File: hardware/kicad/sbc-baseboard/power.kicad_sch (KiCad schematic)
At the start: 86 parts, among them J17 Qwiic PD programming, J2 USB-C PD in, Q101 2N7002, Q102 2N7002, U101 STUSB4500QTR, U102 PCA9517A, U103 TPS54560BDDA, U104 TPS54560BDDA, U105 TPS62823DLC

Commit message: Re-lay out every sheet around its main component
Nets fan out of each hub IC as wires at pin pitch; connectors, series
parts, pull-ups and power symbols sit at the lane ends, and labels are
kept for nets that leave the page. Supply pins share a bus with their
decoupling; ESD arrays sit on the connector's D-/D+ rows and port
switches on the VBUS row, so every wire into a receptacle is straight;
the stacked USB-A is a two-unit symbol, one per port. Relays move to
their own sheet (8xx). ESD diodes use KiCad's PESD5V0S1UL in SOD-882.

Generator: gen/fanout.py (lane engine), gen/check_geom.py (endpoint
contacts), gen/netcheck.py (wire-level rail merges). ERC, both checks
and a renumbering-tolerant netlist diff against the first pass all
clean; 331 parts, 354 nets.

Co-Authored-By: Claude Fable 5.1 <noreply@anthropic.com>
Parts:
- removed C117, C126: 100u/10V, Capacitor_SMD:CP_Elec_8x10.5, symbol Device:C_Polarized
- removed C119, C128: 47u/10V, Capacitor_SMD:C_1210_3225Metric, symbol Device:C
- removed C132: 22u, Capacitor_SMD:C_0805_2012Metric, symbol Device:C
- removed D101: SMAJ24A, Diode_SMD:D_SMA, symbol Diode:SMAJ24A
- removed D102, D110, D112: LED AMBER, LED_SMD:LED_0603_1608Metric, symbol Device:LED
- removed D105: BZT52C5V1, Diode_SMD:D_SOD-123, symbol Device:D_Zener
- removed D106, D107: PESD5V0S1UL, Diode_SMD:D_SOD-523, symbol Device:D_TVS
- removed D108: BAT54C, Package_TO_SOT_SMD:SOT-23, symbol Diode:BAT54C
- removed D111, D113: B560C, Diode_SMD:D_SMA, symbol Device:D_Schottky
- added C117, C126: 47u/10V, Capacitor_SMD:C_1210_3225Metric, symbol Device:C
- added C119, C128: 100u/10V, Capacitor_SMD:CP_Elec_8x10.5, symbol Device:C_Polarized
- added D101: BAT54C, Package_TO_SOT_SMD:SOT-23, symbol Diode:BAT54C
- added D102: ESDA25W, Diode_SMD:D_SOD-523, symbol Device:D_TVS
- added D105, D111, D113: LED AMBER, LED_SMD:LED_0603_1608Metric, symbol Device:LED
- added D106, D107: PESD5V0S1UL, Diode_SMD:D_SOD-882, symbol Diode:PESD5V0S1UL
- added D108: BZT52C5V1, Diode_SMD:D_SOD-123, symbol Device:D_Zener
- added D110, D112: B560C, Diode_SMD:D_SMA, symbol Device:D_Schottky
- C105: value 100n/50V -> 1u
- C108: value 1u -> 100n
- C111: value 100n -> 100n/50V
- C114, C123: value 100n/50V -> 47p
- C116, C125: value 47p -> 100n/50V
- C118, C127: value 100n/50V -> 47u/10V; footprint Capacitor_SMD:C_0603_1608Metric -> Capacitor_SMD:C_1210_3225Metric
- C120: value 47u/10V -> 100n/50V; footprint Capacitor_SMD:C_1210_3225Metric -> Capacitor_SMD:C_0603_1608Metric
- C129: value 47u/10V -> 10u; footprint Capacitor_SMD:C_1210_3225Metric -> Capacitor_SMD:C_0805_2012Metric
- C130: value 10u -> 22u
- D104: value ESDA25W -> SMAJ24A; footprint Diode_SMD:D_SOD-523 -> Diode_SMD:D_SMA
- R103: value 470 -> 10k; footprint Resistor_SMD:R_1206_3216Metric -> Resistor_SMD:R_0603_1608Metric
- R105: value 100k -> 4.7k
- R106: value 10k -> 4.7k
- R108: value 4.7k -> 100k
- R109: value 4.7k -> 470; footprint Resistor_SMD:R_0603_1608Metric -> Resistor_SMD:R_1206_3216Metric
- R110: value 100k -> 10k
- R111, R128: value 470 -> 100k
- R114, R126: value 100k -> 470
- R115: value 10k -> 100k
- R116, R121: value 243k -> 19.1k
- R117, R122: value 19.1k -> 243k
- R118, R123: value 51.1k -> 9.76k
- R119, R124: value 9.76k -> 51.1k
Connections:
- net +3V3: now also C110.1, C130.1, R102.1, R128.2, D101.1; no longer C111.1, R115.1, R128.1
- net +3V3_PD: now also C108.1, R105.1, R110.1, R114.1, D101.3; no longer C110.1, R108.1, R109.1, R111.1
- net +3V3_PRG: now also C107.1, R112.2, R115.1, D101.2; no longer C108.1, R105.1, R112.1
- net +5V_PORTS: now also C118.1, C129.1, R119.2, C117.1, C119.1; no longer C120.1, C130.1, R118.1
- net +5V_TGT: now also C127.1, R124.2, C126.1, C128.1; no longer C129.1, R123.1
- net GND: now also C118.2, C127.2, D103.1 (A1), D104.1 (A1), R103.2, R111.2, R113.2, R117.2, R118.2, R122.2, R123.2, C117.2, C119.2, C126.2, C128.2, D102.1 (A1), D105.1 (K), D106.2 (A), D107.2 (A), D108.2 (A), D110.2 (A), D111.1 (K), D112.2 (A), D113.1 (K); no longer C116.2, C125.2, D103.2 (A2), D104.2 (A2), R102.2, R105.2, R114.2, R116.2, R119.2, R121.2, R124.2
- net PD_ATTACH_N: now also R110.2; no longer R106.2
- net PD_PROG_DET: now also R115.2; no longer R112.2
- net VBUS_IN: now also C111.1, C120.1, D104.2 (A2), R104.2, R108.1, R109.2; no longer C105.1, C114.1, C123.1, R103.1, R104.1, R110.1
- net at D114.2 (A): now also R126.2; no longer R128.2
- net at R101.2: now also D105.2 (A)
- net at D109.2 (A): now also R114.2; no longer R111.2
- net at R125.2: now also D113.2 (A)
- net at R120.2: now also D111.2 (A)
- net PCA_EN: no longer names the net of Q102.3 (D), U102.5 (EN)
- net PCA_EN: now also R102.2; no longer R115.2
- removed net PCA_EN_GATE: Q102.1 (G), R113.2, R114.1
- net PD_CC1: no longer names the net of J2.A5 (CC1), U101.1 (CC1DB), U101.2 (CC1)
- net PD_CC1: now also D102.2 (A2); no longer D103.1 (A1)
- net PD_CC2: no longer names the net of J2.B5 (CC2), U101.4 (CC2), U101.5 (CC2DB)
- net PD_CC2: now also D103.2 (A2); no longer D104.1 (A1)
- net PD_DISCH: no longer names the net of U101.9 (DISCH)
- net PD_DISCH: now also R109.1; no longer R103.2
- net PD_RESET: no longer names the net of U101.6 (RESET)
- net PD_RESET: now also R103.1; no longer R102.1
- net PD_SCL: no longer names the net of J17.4 (Pin_4), U101.7 (SCL), U102.2 (SCLA)
- net PD_SCL: now also R105.2, D106.1 (K); no longer R108.2
- net PD_SDA: no longer names the net of J17.3 (Pin_3), U101.8 (SDA), U102.3 (SDAA)
- net PD_SDA: now also R106.2, D107.1 (K); no longer R109.2
- net PD_VBUS_EN_N: no longer names the net of Q101.1 (G), U101.16 (VBUS_EN_SNK)
- net PD_VBUS_EN_N: now also R108.2, D108.1 (K); no longer R110.2
- net PD_VBUS_VS: no longer names the net of U101.18 (VBUS_VS_DISCH)
- net PD_VBUS_VS: now also R104.1; no longer R104.2
- net PD_VREG_1V2: no longer names the net of U101.21 (VREG_1V2)
- net PD_VREG_1V2: now also C105.1; no longer C106.1
- net PD_VREG_2V7: no longer names the net of U101.23 (VREG_2V7)
- net PD_VREG_2V7: now also C106.1; no longer C107.1
- net U103_BOOT: no longer names the net of U103.1 (BOOT)
- net U103_BOOT: now also C116.1; no longer C118.1
- removed net U103_COMP: C116.1, R117.1, U103.6 (COMP)
- net U103_CZ: no longer names the net of C115.1
- net U103_CZ: now also R116.2; no longer R117.2
- net U103_FB: no longer names the net of R119.1, U103.5 (FB)
- net U103_FB: now also R118.1; no longer R118.2
- net U103_RT: no longer names the net of R116.1
- net U103_RT: now also C114.1, U103.6 (COMP); no longer U103.4 (RT/CLK)
- net U103_SW: no longer names the net of L101.1, U103.8 (SW)
- net U103_SW: now also C116.2, D110.1 (K); no longer C118.2
- net U104_BOOT: no longer names the net of U104.1 (BOOT)
- net U104_BOOT: now also C125.1; no longer C127.1
- removed net U104_COMP: C125.1, R122.1, U104.6 (COMP)
- net U104_CZ: no longer names the net of C124.1
- net U104_CZ: now also R121.2; no longer R122.2
- net U104_FB: no longer names the net of R124.1, U104.5 (FB)
- net U104_FB: now also R123.1; no longer R123.2
- net U104_RT: no longer names the net of R121.1
- net U104_RT: now also C123.1, U104.6 (COMP); no longer U104.4 (RT/CLK)
- net U104_SW: no longer names the net of L102.1, U104.8 (SW)
- net U104_SW: now also C125.2, D112.1 (K); no longer C127.2
- net U105_FB: no longer names the net of R127.1, U105.2 (FB)
- net U105_FB: now also R128.1; no longer R126.2
- net U105_SW: no longer names the net of L103.1, U105.6 (SW)
- new net: Q102.1 (G), R111.1, R112.1
- new net: R117.1, U103.4 (RT/CLK)
- new net: R122.1, U104.4 (RT/CLK)
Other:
- note added: "A programmer on J17 pulls PCA_EN low through Q102: the K64 is disconnected from the PD bus in hardware."
- note added: "J2 is a PD sink only (no data). STUSB4500 negotiates from NVM; VBUS_EN_SNK gates the 5 V bucks through Q101,"
- note added: "The zener keeps the gate under 5.1 V at 20 V VBUS."
- note removed: "A programmer on J17 pulls PCA_EN low: the K64 is disconnected from the PD bus in hardware."
- note removed: "Buck 1 feeds the USB ports, the FT231X, the relay coils and buck 3 (~4.6 A at 1.0 A/port); buck 2 is the 5 A target rail."
- note removed: "J2 is a PD sink only (no data). STUSB4500 negotiates from NVM; VBUS_EN_SNK gates the 5 V bucks,"
- note removed: "Zener keeps the gate below 5.1 V at 20 V VBUS."

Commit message: Symbol direction, field text and decoupling ladders across every sheet
Every GND symbol now hangs down and every rail stands up: decoupling
hangs from the supply bus into a GND rail with one GND symbol at the end
(ladders), rails on crowded supply pins are jogged sideways, the SWD
header is mirrored instead of rotated. Field text on in-line parts reads
horizontally (KiCad adds the symbol rotation to the field angle) and is
placed by lane direction; hanging parts carry their text on the side away
from the pin; IC reference and value sit where the library put them.
Power sheet: bus buffer moved under the STUSB4500's I2C lanes with direct
routes, programmer by label, buck drawn as a box with its input and
output capacitors as ladders. New gen/check_layout.py reports text and
wire overlaps and wrong-way power symbols; PDF export draws hop-overs.

ERC 0, no merged rails, netlist equivalent; text-overlap residue listed
in the layout checker output remains on the hub, relays and DAPLink.

Co-Authored-By: Claude Fable 5.1 <noreply@anthropic.com>
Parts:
- removed U103, U104: TPS54560BDDA, Package_SO:HSOP-8-1EP_3.9x4.9mm_P1.27mm_EP2.41x3.1mm, symbol Regulator_Switching:TPS54560BDDA
- added U103, U104: TPS54560BDDA, Package_SO:HSOP-8-1EP_3.9x4.9mm_P1.27mm_EP2.41x3.1mm, symbol sbcbb:TPS54560BDDA
- R103: value 10k -> 1k
- R104: value 1k -> 4.7k
- R106: value 4.7k -> 10k
- R107: value 10k -> 100k
- R108: value 100k -> 470; footprint Resistor_SMD:R_0603_1608Metric -> Resistor_SMD:R_1206_3216Metric
- R109: value 470 -> 10k; footprint Resistor_SMD:R_1206_3216Metric -> Resistor_SMD:R_0603_1608Metric
- R116, R121: value 19.1k -> 243k
- R117, R122: value 243k -> 19.1k
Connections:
- net +3V3: now also R110.1; no longer R102.1
- net +3V3_PD: now also R104.1, R109.1; no longer R107.1, R110.1
- net BUCK_EN: now also U103.3 (EN), U104.3 (EN)
- net GND: now also R102.2, R116.2, R121.2, U103.7 (GND), U103.9 (PAD), U104.7 (GND), U104.9 (PAD); no longer R103.2, R117.2, R122.2
- net PD_ALERT_N: now also R106.2; no longer R107.2
- net PD_ATTACH_N: now also R109.2; no longer R110.2
- net VBUS_IN: now also R103.2, R107.1, R108.2, U103.2 (VIN), U104.2 (VIN); no longer R104.2, R108.1, R109.2
- net at D108.1 (K), Q101.1 (G), U101.16 (VBUS_EN_SNK): now also R107.2; no longer R108.2
- net at U101.18 (VBUS_VS_DISCH): now also R103.1; no longer R104.1
- net at U101.6 (RESET): now also R102.1; no longer R103.1
- net PD_SCL: now reaches D106.1 (K), J17.4 (Pin_4), U101.7 (SCL), U102.2 (SCLA)
- net PD_SCL: now also R104.2; no longer R105.2
- net PD_SDA: now reaches D107.1 (K), J17.3 (Pin_3), U101.8 (SDA), U102.3 (SDAA)
- net PD_SDA: now also R105.2; no longer R106.2
- net at U101.9 (DISCH): now also R108.1; no longer R109.1
- net at Q102.3 (D), U102.5 (EN): now also R110.2; no longer R102.2
- net at C123.1: now also R122.1, U104.6 (COMP); no longer R121.1
- net at C124.1: now also R122.2; no longer R121.2
- net at C116.2, D110.1 (K), L101.1: now also U103.8 (SW)
- net at R118.1, R119.1: now also U103.5 (FB)
- net at C125.2, D112.1 (K), L102.1: now also U104.8 (SW)
- net at C114.1: now also R117.1, U103.6 (COMP); no longer R116.1
- net at C115.1: now also R117.2; no longer R116.2
- net at R123.1, R124.1: now also U104.5 (FB)
- net at C116.1: now also U103.1 (BOOT)
- net at C125.1: now also U104.1 (BOOT)
- new net: R121.1, U104.4 (RT/CLK)
- new net: R116.1, U103.4 (RT/CLK)

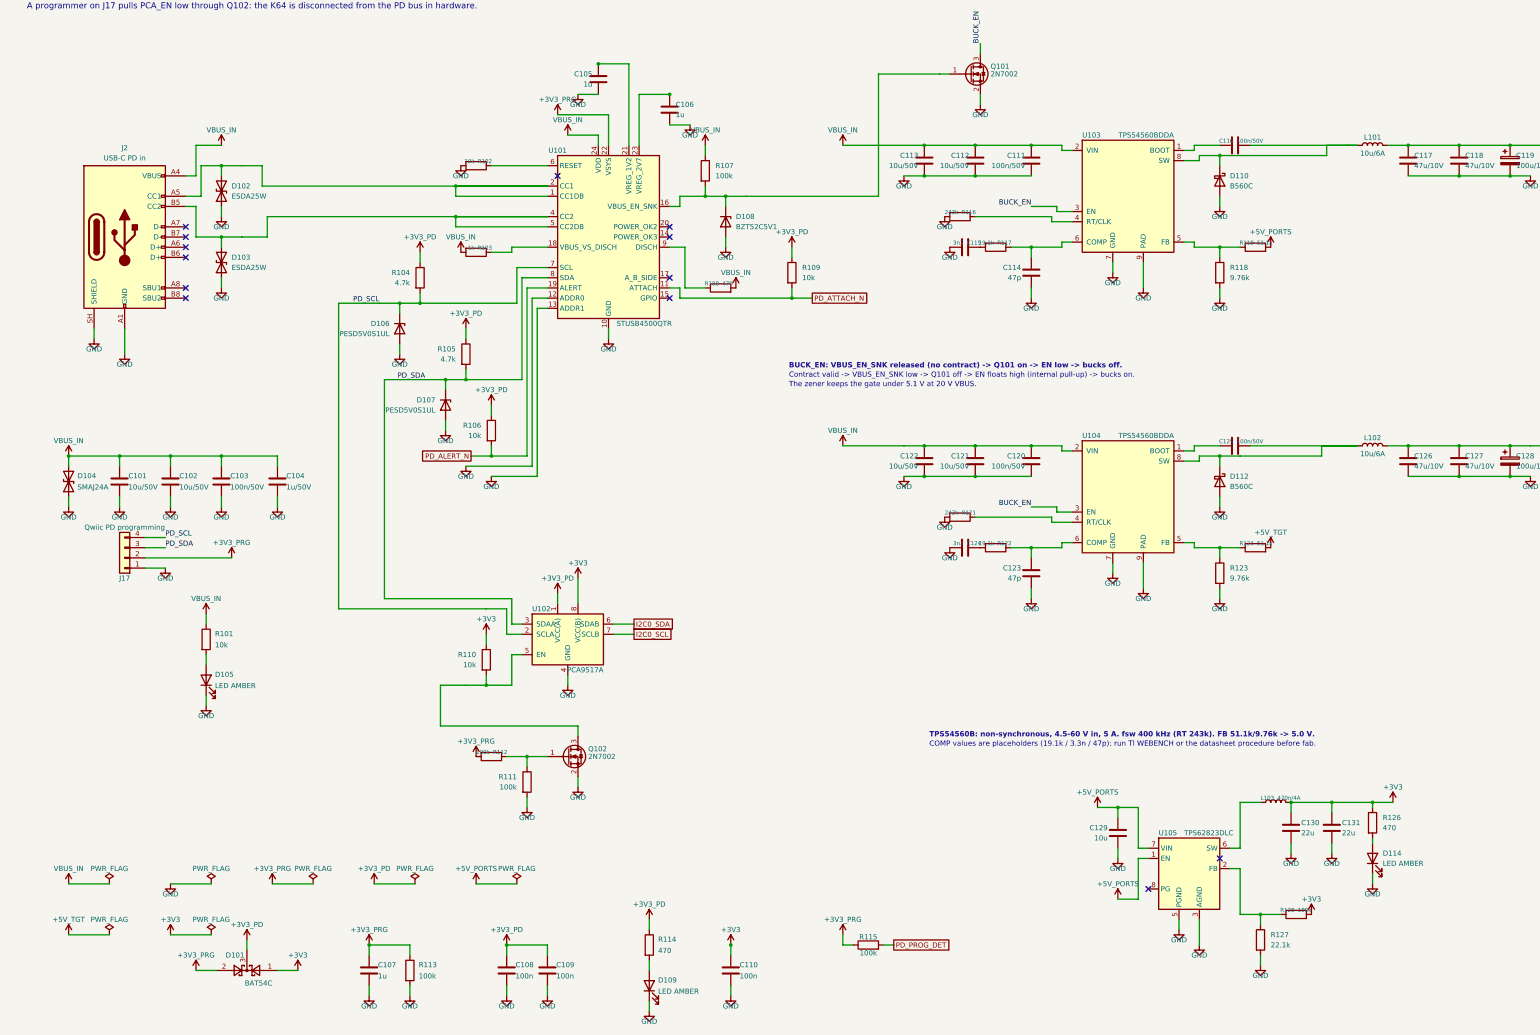
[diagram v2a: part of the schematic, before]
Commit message: Placement pass: every sheet clean on all four layout gates
Hanging parts now sit with their near pin between rows, so a pull-up on
the next lane crosses only its lead; parts slide past a neighbour's parts
and text, not its plain wire, and never let a wire run through a body or
a rail symbol. Chains on top/bottom pins run sideways first. Route
channels are numbered per route. Power symbols that would land on a
neighbouring wire get a jog or a hook. The VBUS sense divider moved to
the K64's ADC pin so J3's VBUS lane is a short stretch the ESD array taps;
the J1 tap sits before its divider. Relay coil clusters are drawn by the
engine. Port switches moved so OUT stays on the VBUS row.

ERC 0, no endpoint contacts, no merged rails, no wires through bodies,
no inverted power symbols, on all eight sheets; netlist equivalent to the
first pass (331 parts, 354 nets); USB D+/D-, VBUS and I2C paths verified
pin by pin.

Co-Authored-By: Claude Fable 5.1 <noreply@anthropic.com>
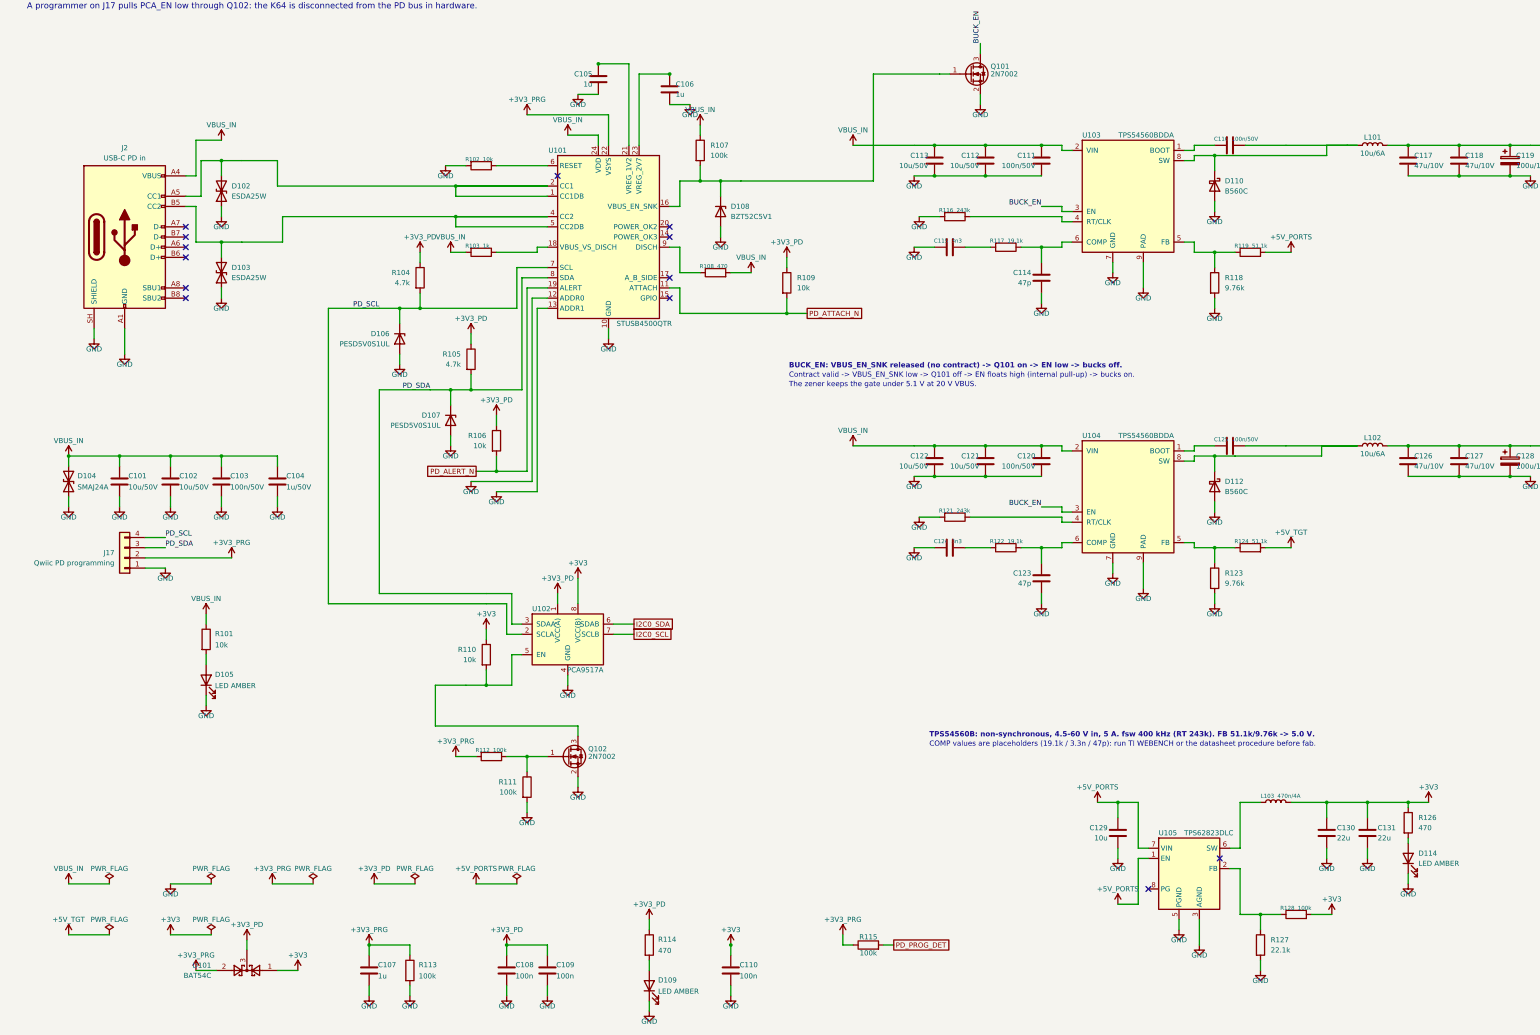
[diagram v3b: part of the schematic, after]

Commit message: Symbol name clearance, divider at the reading pin, inlet TVS orientation
Symbols: a top or bottom pin's name runs vertically into the body, so box
symbols now grow outward by whole rows wherever such a name would reach a
side pin's name (USB2517 three rows on top, K64 two rows top and bottom,
PCA9517A three rows on top); the side-pin rows stay where they were so the
sheet layouts are unaffected. U402's VDD names no longer print over USBUP_DP.

Frame pass: nothing on the sheet frame or the title block, enforced by the
layout gate (usable area 15..405 x 15..282 mm, title block from 300/253).

Flow pass: pull-ups hang up to their rail, pull-downs hang down (R408/R409
and the other strap and sense resistors). The J1 VBUS_DET divider sits at
U402 pin 44, the pin that reads it; J1's VBUS lane is a plain stretch that
U401 taps; J1 and U401 lifted clear of the hub's +3V3 bus. The hub's left
strap lanes turn in columns starting at x = 118.11 so they clear the bottom
decoupling ladders (fan() grew a turn_at argument for this).

Inlet TVS D102 hangs from J2's VBUS lane as a D_Zener with its cathode on
VBUS_IN. At 8579cd2 it was drawn with the bidirectional D_TVS symbol and
pad 1 (the SMA cathode) on GND, which would have forward-biased it.

Bucks: the FB pulls start past the catch diode's text; the two notes are
rewrapped and sit between U101 and the compensation parts.

Gates on every sheet: ERC 0, endpoint contacts 0, rail merges 0, frame 0,
no text on bodies or wires. Connectivity identical to 8579cd2 (symmetric
passives order-free) except the TVS orientation.

Co-Authored-By: Claude Fable 5.1 <noreply@anthropic.com>
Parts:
- removed D102: ESDA25W, Diode_SMD:D_SOD-523, symbol Device:D_TVS
- added D102: SMAJ24A, Diode_SMD:D_SMA, symbol Device:D_Zener
- D104: value SMAJ24A -> ESDA25W; footprint Diode_SMD:D_SMA -> Diode_SMD:D_SOD-523
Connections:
- net +3V3: now also R128.1; no longer R128.2
- net +5V_PORTS: now also R119.1; no longer R119.2
- net +5V_TGT: now also R124.1; no longer R124.2
- net GND: now also D102.2 (A)
- net VBUS_IN: now also R108.1, D102.1 (K); no longer D104.2 (A2), R108.2
- net at R118.1, U103.5 (FB): now also R119.2; no longer R119.1
- net at R127.1, U105.2 (FB): now also R128.2; no longer R128.1
- net at R123.1, U104.5 (FB): now also R124.2; no longer R124.1
- net at J2.A5 (CC1), U101.1 (CC1DB), U101.2 (CC1): now also D103.2 (A2)
- net at J2.B5 (CC2), U101.4 (CC2), U101.5 (CC2DB): now also D104.2 (A2); no longer D103.2 (A2)
- net at U101.9 (DISCH): now also R108.2; no longer R108.1
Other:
- note added: "-> EN low -> bucks off. Contract valid -> VBUS_EN_SNK low"
- note added: "-> Q101 off -> EN floats high (internal pull-up) -> bucks on."
- note added: "BUCK_EN: VBUS_EN_SNK released (no contract) -> Q101 on"
- note added: "FB 51.1k/9.76k -> 5.0 V. COMP values are placeholders (19.1k / 3.3n / 47p):"
- note added: "TPS54560B: non-synchronous, 4.5-60 V in, 5 A. fsw 400 kHz (RT 243k)."
- note added: "run TI WEBENCH or the datasheet procedure before fab."
- note removed: "BUCK_EN: VBUS_EN_SNK released (no contract) -> Q101 on -> EN low -> bucks off."
- note removed: "COMP values are placeholders (19.1k / 3.3n / 47p): run TI WEBENCH or the datasheet procedure before fab."
- note removed: "Contract valid -> VBUS_EN_SNK low -> Q101 off -> EN floats high (internal pull-up) -> bucks on."
- note removed: "TPS54560B: non-synchronous, 4.5-60 V in, 5 A. fsw 400 kHz (RT 243k). FB 51.1k/9.76k -> 5.0 V."
